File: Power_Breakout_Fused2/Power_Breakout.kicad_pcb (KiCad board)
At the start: 2 copper layers, 85.5 x 41.5 mm, 18 parts, among them J1 PS Conn, J2 Conn_01x02_Male, J3 PWR Out, J4 GND Out

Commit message: Generated Gerbers
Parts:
- moved REF** 1.44 mm to (191.9, 136.2), turned to 180 degrees
- turned REF** to 180 degrees
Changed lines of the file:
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@@
     (property "Sheetname" "")
     (attr through_hole)
-    (fp_text reference "J1" (at -42.116 -5.3014) (layer "F.SilkS")
-      (effects (font (size 0.640546 0.640546) (thickness 0.015)))
+    (fp_text reference "J1" (at -41.816 -5.7014 180 unlocked) (layer "F.SilkS")
+      (effects (font (size 1 1) (thickness 0.15)))
     )
     (fp_text value "PS Conn" (at -36.068 -5.588) (layer "F.Fab")
@@
       (net 1 "+12V") (pinfunction "Pin_64") (pintype "passive"))
     (model "${GIT_MODELS}/10046971001LFc.stp"
-      (offset (xyz 0 0 0))
+      (offset (xyz 0 0 5.5))
       (scale (xyz 1 1 1))
-      (rotate (xyz 0 0 0))
+      (rotate (xyz -90 0 0))
     )
   )
   (footprint "Symbol:OSHW-Logo2_9.8x8mm_SilkScreen" (layer "F.Cu")
-    (at 192.3 137.65)
+    (at 191.95 136.25 180)
     (descr "Open Source Hardware Symbol")
     (tags "Logo Symbol OSHW")
     (attr exclude_from_pos_files exclude_from_bom)
-    (fp_text reference "REF**" (at 0 0) (layer "F.SilkS") hide
+    (fp_text reference "REF**" (at -0.25 -1.35) (layer "F.SilkS") hide
       (effects (font (size 1 1) (thickness 0.15)))
     )
@@
       (effects (font (size 1 1) (thickness 0.15)))
     )
-    (fp_text value "GND Out" (at 17.8125 -5.9) (layer "F.SilkS")
+    (fp_text value "GND Out" (at 17.8125 -5.9 180 unlocked) (layer "F.SilkS")
       (effects (font (size 1.5 1.5) (thickness 0.3)))
     )
@@
     (pad "8" thru_hole oval (at 35.56 0) (size 1.8 3.6) (drill 1.2) (layers *.Cu *.Mask)
       (net 2 "GND") (pinfunction "Pin_8") (pintype "passive"))
-    (model "${KICAD6_3DMODEL_DIR}/Connector_Phoenix_MC_HighVoltage.3dshapes/PhoenixContact_MCV_1,5_8-G-5.08_1x08_P5.08mm_Vertical.wrl"
+    (model "${KICAD6_3DMODEL_DIR}/Connector_Phoenix_MC_HighVoltage.3dshapes/PhoenixContact_MCV_1,5_8-G-5.08_1x08_P5.08mm_Vertical.wrl" hide
       (offset (xyz 0 0 0))
       (scale (xyz 1 1 1))
       (rotate (xyz 0 0 0))
     )
+    (model "${KIPRJMOD}/libraries/3D Models/282834-8--3DModel-STEP-1.STEP"
+      (offset (xyz 17.5 5.5 3))
+      (scale (xyz 2 1 1.5))
+      (rotate (xyz -90 0 180))
+    )
   )
   (footprint "Symbol:KiCad-Logo2_6mm_SilkScreen" (layer "F.Cu")
-    (at 174.05 136.9)
+    (at 174.05 136.9 180)
     (descr "KiCad Logo")
     (tags "Logo KiCad")
@@
       (effects (font (size 1 1) (thickness 0.15)))
     )
-    (fp_text value "PWR Out" (at 17.85 -6.05) (layer "F.SilkS")
+    (fp_text value "PWR Out" (at 17.85 -6.05 180 unlocked) (layer "F.SilkS")
       (effects (font (size 1.5 1.5) (thickness 0.3)))
     )
@@
     (pad "8" thru_hole oval (at 35.56 0) (size 1.8 3.6) (drill 1.2) (layers *.Cu *.Mask)
       (net 10 "Net-(F8-Pad2_1)") (pinfunction "Pin_8") (pintype "passive"))
-    (model "${KICAD6_3DMODEL_DIR}/Connector_Phoenix_MC_HighVoltage.3dshapes/PhoenixContact_MCV_1,5_8-G-5.08_1x08_P5.08mm_Vertical.wrl"
+    (model "${KICAD6_3DMODEL_DIR}/Connector_Phoenix_MC_HighVoltage.3dshapes/PhoenixContact_MCV_1,5_8-G-5.08_1x08_P5.08mm_Vertical.wrl" hide
       (offset (xyz 0 0 0))
       (scale (xyz 1 1 1))
       (rotate (xyz 0 0 0))
     )
+    (model "${KIPRJMOD}/libraries/3D Models/282834-8--3DModel-STEP-1.STEP"
+      (offset (xyz 17 5.5 3))
+      (scale (xyz 2 1 1.5))
+      (rotate (xyz -90 0 180))
+    )
   )
   (footprint "3544-2:FUSE_3544-2" (layer "F.Cu")
@@
     (property "Sheetname" "")
     (attr through_hole)
-    (fp_text reference "F8" (at -8.18321 -1.55 180) (layer "F.SilkS")
+    (fp_text reference "F8" (at -8.18321 -1.55) (layer "F.SilkS")
       (effects (font (size 1 1) (thickness 0.05)))
     )
@@
     (property "Sheetname" "")
     (attr through_hole)
-    (fp_text reference "J2" (at 0 -2.33) (layer "F.SilkS")
+    (fp_text reference "J2" (at 0 5.075 180 unlocked) (layer "F.SilkS")
       (effects (font (size 1 1) (thickness 0.15)))
     )
@@
     (pad "2" thru_hole oval (at 0 2.54 180) (size 1.7 1.7) (drill 1) (layers *.Cu *.Mask)
       (net 24 "Net-(J2-Pad2)") (pinfunction "Pin_2") (pintype "passive"))
-    (model "${KICAD6_3DMODEL_DIR}/Connector_PinHeader_2.54mm.3dshapes/PinHeader_1x02_P2.54mm_Vertical.wrl"
+    (model "${KICAD6_3DMODEL_DIR}/Connector_PinHeader_2.54mm.3dshapes/PinHeader_1x02_P2.54mm_Vertical.wrl" hide
       (offset (xyz 0 0 0))
       (scale (xyz 1 1 1))
@@
   (gr_line (start 202.6158 161.9758) (end 202.6158 120.5) (layer "Edge.Cuts") (width 0.05))
   (gr_line (start 202.6158 120.5) (end 117.1194 120.5) (layer "Edge.Cuts") (width 0.05))
-  (gr_text "${TITLE} ${REVISION}\nby ${COMPANY}" (at 176.35 147.8) (layer "F.SilkS")
+  (gr_text "${TITLE} ${REVISION}\nby ${COMPANY}" (at 178.3 144.05 180) (layer "F.SilkS")
     (effects (font (size 1.5 1.5) (thickness 0.3)))
   )
@@
         (xy 202.65 162.45)
         (xy 152.6 162.4)
-        (xy 152.6 154.2)
-        (xy 160.05 154.2)
+        (xy 152.6 153.5)
+        (xy 160.05 153.5)
         (xy 160.05 120.5)
       )
@@
     (polygon
       (pts
-        (xy 159.2 153.2)
-        (xy 152.05 153.2)
+        (xy 159.2 152.75)
+        (xy 152.05 152.75)
         (xy 152.048439 162.476089)
         (xy 116.9 162.526089)

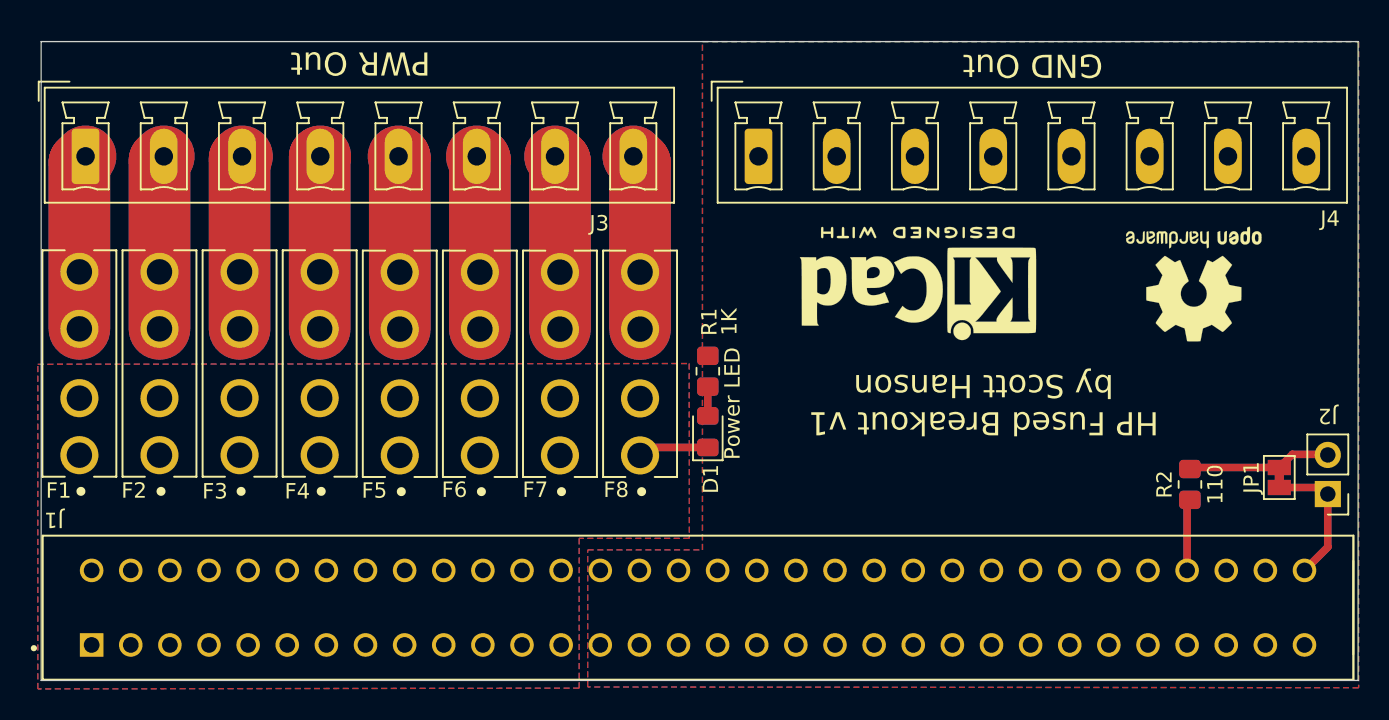
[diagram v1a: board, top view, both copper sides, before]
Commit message: added more leds
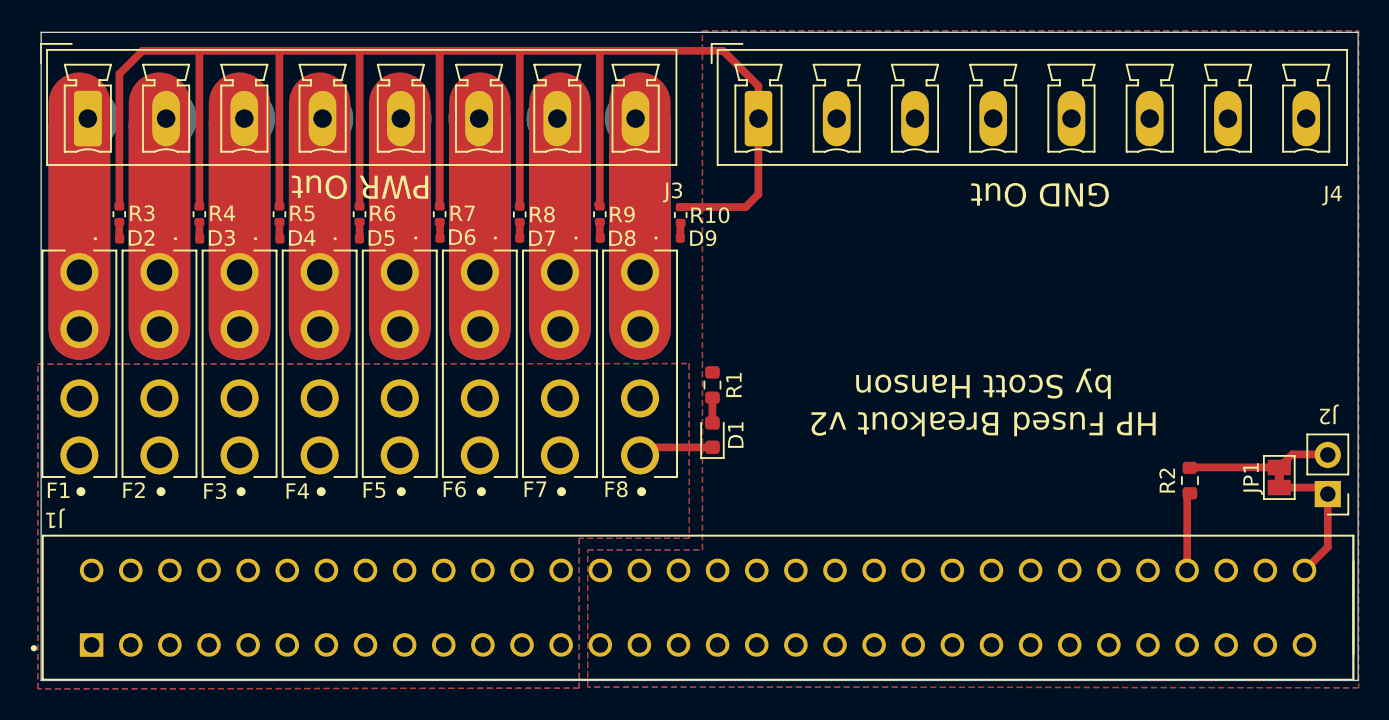
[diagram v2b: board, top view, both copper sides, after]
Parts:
- removed REF**: OSHW-Logo2_9.8x8mm_SilkScreen, Symbol:OSHW-Logo2_9.8x8mm_SilkScreen
- removed REF**: KiCad-Logo2_6mm_SilkScreen, Symbol:KiCad-Logo2_6mm_SilkScreen
- added D2: LED, LED_SMD:LED_0402_1005Metric, F.Cu at (121.7, 133.3)
- added D3: LED, LED_SMD:LED_0402_1005Metric, F.Cu at (126.9, 133.3)
- added D4: LED, LED_SMD:LED_0402_1005Metric, F.Cu at (132.1, 133.3)
- added D5: LED, LED_SMD:LED_0402_1005Metric, F.Cu at (137.3, 133.3)
- added D6: LED, LED_SMD:LED_0402_1005Metric, F.Cu at (142.5, 133.2)
- added D7: LED, LED_SMD:LED_0402_1005Metric, F.Cu at (147.7, 133.2)
- added D8: LED, LED_SMD:LED_0402_1005Metric, F.Cu at (152.9, 133.2)
- added D9: LED, LED_SMD:LED_0402_1005Metric, F.Cu at (158.1, 133.2)
- added R10: 2.2K, Resistor_SMD:R_0402_1005Metric, F.Cu at (158.6, 131.8)
- added R3: 2.2K, Resistor_SMD:R_0402_1005Metric, F.Cu at (122.2, 131.7)
- added R4: 2.2K, Resistor_SMD:R_0402_1005Metric, F.Cu at (127.4, 131.7)
- added R5: 2.2K, Resistor_SMD:R_0402_1005Metric, F.Cu at (132.6, 131.7)
- added R6: 2.2K, Resistor_SMD:R_0402_1005Metric, F.Cu at (137.8, 131.7)
- added R7: 2.2K, Resistor_SMD:R_0402_1005Metric, F.Cu at (143.0, 131.7)
- added R8: 2.2K, Resistor_SMD:R_0402_1005Metric, F.Cu at (148.2, 131.7)
- added R9: 2.2K, Resistor_SMD:R_0402_1005Metric, F.Cu at (153.4, 131.7)
- D1: footprint LED_SMD:LED_0805_2012Metric_Pad1.15x1.40mm_HandSolder -> LED_SMD:LED_0603_1608Metric
- R1: value 1K -> 2.2K; footprint Resistor_SMD:R_0805_2012Metric_Pad1.20x1.40mm_HandSolder -> Resistor_SMD:R_0603_1608Metric
- R2: value 110 -> 100; footprint Resistor_SMD:R_0805_2012Metric_Pad1.20x1.40mm_HandSolder -> Resistor_SMD:R_0603_1608Metric
- moved J3 2.45 mm to (120.2, 125.5)
- moved J4 2.45 mm to (163.7, 125.5)
- moved R1 0.95 mm to (160.7, 142.8)
- moved D1 0.38 mm to (160.7, 146.1)
- moved R2 0.25 mm to (191.7, 149.0)
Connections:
- net Net-(F1-Pad2_1) renamed PWR1
- net Net-(F2-Pad2_1) renamed PWR2
- net Net-(F3-Pad2_1) renamed PWR3
- net Net-(F4-Pad2_1) renamed PWR4
- net Net-(F5-Pad2_1) renamed PWR5
- net Net-(F6-Pad2_1) renamed PWR6
- net Net-(F7-Pad2_1) renamed PWR7
- net Net-(F8-Pad2_1) renamed PWR8
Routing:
- net GND: track 0.00 -> 125.1 mm
- net PWR4: track 22.4 -> 28.4 mm
- net PWR3: track 22.5 -> 28.4 mm
- net PWR2: track 22.6 -> 28.5 mm
- net PWR5: track 22.5 -> 28.4 mm
- net PWR1: track 22.7 -> 28.5 mm
- net PWR6: track 22.6 -> 28.4 mm
- net PWR7: track 22.7 -> 28.4 mm
- net PWR8: track 22.8 -> 28.5 mm
- net Net-(D4-A): track 0.00 -> 1.09 mm
- net Net-(D3-A): track 0.00 -> 1.09 mm
- net Net-(D2-A): track 0.00 -> 1.09 mm
- net Net-(D5-A): track 0.00 -> 1.08 mm
- net Net-(D8-A): track 0.00 -> 1.04 mm
- net Net-(D6-A): track 0.00 -> 1.04 mm
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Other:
- board size 85.5 x 41.5 mm -> 85.5 x 42.1 mm
- board text added: "GND Out"
- board text added: "PWR Out"

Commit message: move header
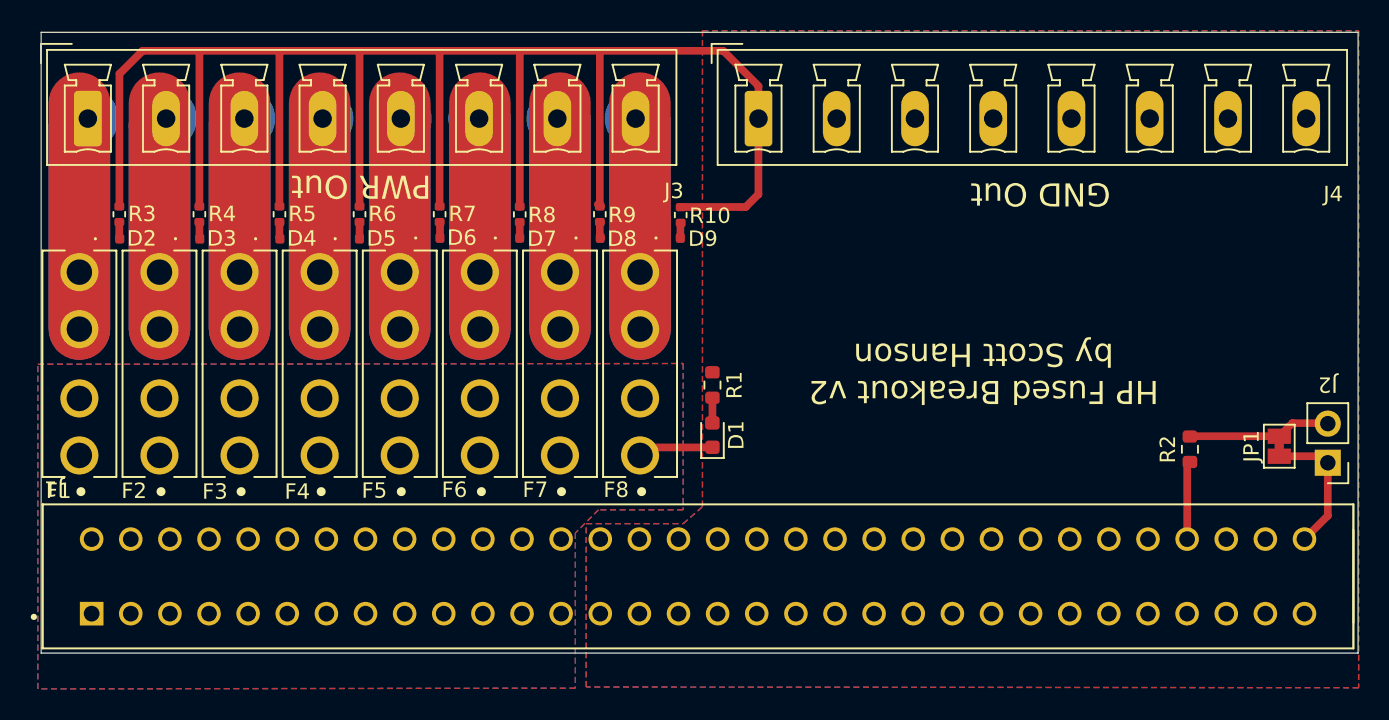
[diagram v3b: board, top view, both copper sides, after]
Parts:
- moved JP1 2.03 mm to (197.5, 146.8)
- moved J1 2.03 mm to (159.8, 155.2)
- moved J2 2.03 mm to (200.7, 147.8)
- moved R2 2.03 mm to (191.7, 147.0)
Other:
- board size 85.5 x 42.1 mm -> 85.5 x 40.3 mm
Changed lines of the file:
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@@
 	(footprint "Resistor_SMD:R_0603_1608Metric"
 		(layer "F.Cu")
-		(at 191.7 149 90)
+		(at 191.7 146.9686 90)
 		(descr "Resistor SMD 0603 (1608 Metric), square (rectangular) end terminal, IPC_7351 nominal, (Body size source: IPC-SM-782 page 72, https://www.pcb-3d.com/wordpress/wp-content/uploads/ipc-sm-782a_amendment_1_and_2.pdf), generated with kicad-footprint-generator")
 		(tags "resistor")
@@
 	(footprint "TE_1761469-1:TE_1761469-1"
 		(layer "F.Cu")
-		(at 159.766 157.2514)
+		(at 159.766 155.22)
 		(property "Reference" "J1"
 			(at -41.816 -5.7014 180)
@@
 		(tags "LED")
 		(property "Reference" "D3"
-			(at 1.91 -0.02 360)
+			(at 1.91 -0.02 0)
 			(layer "F.SilkS")
 			(effects
@@
 		)
 		(property "Value" "LED"
-			(at 0 1.17 360)
+			(at 0 1.17 0)
 			(layer "F.Fab")
 			(effects
@@
 		)
 		(fp_text user "${REFERENCE}"
-			(at 0 0 360)
+			(at 0 0 0)
 			(layer "F.Fab")
 			(effects
@@
 		(tags "LED")
 		(property "Reference" "D2"
-			(at 1.91 -0.02 360)
+			(at 1.91 -0.02 0)
 			(layer "F.SilkS")
 			(effects
@@
 		)
 		(property "Value" "LED"
-			(at 0 1.17 360)
+			(at 0 1.17 0)
 			(layer "F.Fab")
 			(effects
@@
 		)
 		(fp_text user "${REFERENCE}"
-			(at 0 0 360)
+			(at 0 0 0)
 			(layer "F.Fab")
 			(effects
@@
 		(tags "LED")
 		(property "Reference" "D5"
-			(at 1.91 -0.02 360)
+			(at 1.91 -0.02 0)
 			(layer "F.SilkS")
 			(effects
@@
 		)
 		(property "Value" "LED"
-			(at 0 1.17 360)
+			(at 0 1.17 0)
 			(layer "F.Fab")
 			(effects
@@
 		)
 		(fp_text user "${REFERENCE}"
-			(at 0 0 360)
+			(at 0 0 0)
 			(layer "F.Fab")
 			(effects
@@
 		(tags "LED")
 		(property "Reference" "D8"
-			(at 1.9 0.05 360)
+			(at 1.9 0.05 0)
 			(layer "F.SilkS")
 			(effects
@@
 		)
 		(property "Value" "LED"
-			(at 0 1.17 360)
+			(at 0 1.17 0)
 			(layer "F.Fab")
 			(effects
@@
 		)
 		(fp_text user "${REFERENCE}"
-			(at 0 0 360)
+			(at 0 0 0)
 			(layer "F.Fab")
 			(effects
@@
 		(tags "LED")
 		(property "Reference" "D4"
-			(at 1.91 -0.02 360)
+			(at 1.91 -0.02 0)
 			(layer "F.SilkS")
 			(effects
@@
 		)
 		(property "Value" "LED"
-			(at 0 1.17 360)
+			(at 0 1.17 0)
 			(layer "F.Fab")
 			(effects
@@
 		)
 		(fp_text user "${REFERENCE}"
-			(at 0 0 360)
+			(at 0 0 0)
 			(layer "F.Fab")
 			(effects
@@
 	(footprint "Connector_PinHeader_2.54mm:PinHeader_1x02_P2.54mm_Vertical"
 		(layer "F.Cu")
-		(at 200.65 149.875 180)
+		(at 200.65 147.8436 180)
 		(descr "Through hole straight pin header, 1x02, 2.54mm pitch, single row")
 		(tags "Through hole pin header THT 1x02 2.54mm single row")
@@
 	(footprint "Jumper:SolderJumper-2_P1.3mm_Bridged_Pad1.0x1.5mm"
 		(layer "F.Cu")
-		(at 197.5 148.8 90)
+		(at 197.5 146.7686 90)
 		(descr "SMD Solder Jumper, 1x1.5mm Pads, 0.3mm gap, bridged with 1 copper strip")
 		(tags "net tie solder jumper bridged")
@@
 		(tags "LED")
 		(property "Reference" "D7"
-			(at 1.9325 0.05 360)
+			(at 1.9325 0.05 0)
 			(layer "F.SilkS")
 			(effects
@@
 		)
 		(property "Value" "LED"
-			(at 0 1.17 360)
+			(at 0 1.17 0)
 			(layer "F.Fab")
 			(effects
@@
 		)
 		(fp_text user "${REFERENCE}"
-			(at 0 0 360)
+			(at 0 0 0)
 			(layer "F.Fab")
 			(effects
@@
 	(gr_line
 		(start 117.1194 119.9)
-		(end 117.1194 161.9758)
+		(end 117.1194 160.2)
 		(stroke
 			(width 0.05)
@@
 	)
 	(gr_line
-		(start 117.1194 161.9758)
-		(end 202.6158 161.9758)
+		(start 117.1194 160.2)
+		(end 202.6158 160.2)
 		(stroke
 			(width 0.05)
@@
 	)
 	(gr_line
-		(start 202.6158 161.9758)
+		(start 202.6158 160.2)
 		(end 202.6158 119.9)
 		(stroke
@@
 	)
 	(gr_text "${TITLE} ${REVISION}\nby ${COMPANY}"
-		(at 178.3 144.05 180)
+		(at 178.3 142.0186 180)
 		(layer "F.SilkS")
 		(effects
@@
 	)
 	(segment
-		(start 191.516 154.8314)
-		(end 191.516 150.009)
+		(start 191.516 152.8)
+		(end 191.516 147.9776)
 		(width 0.5)
 		(layer "F.Cu")
@@
 	)
 	(segment
-		(start 191.516 150.009)
-		(end 191.7 149.825)
+		(start 191.516 147.9776)
+		(end 191.7 147.7936)
 		(width 0.5)
 		(layer "F.Cu")
@@
 	)
 	(segment
-		(start 200.65 153.3174)
-		(end 199.136 154.8314)
+		(start 200.65 151.286)
+		(end 199.136 152.8)
 		(width 0.5)
 		(layer "F.Cu")
@@
 	)
 	(segment
-		(start 197.5 149.45)
-		(end 200.225 149.45)
+		(start 197.5 147.4186)
+		(end 200.225 147.4186)
 		(width 0.5)
 		(layer "F.Cu")
@@
 	)
 	(segment
-		(start 200.225 149.45)
-		(end 200.65 149.875)
+		(start 200.225 147.4186)
+		(end 200.65 147.8436)
 		(width 0.5)
 		(layer "F.Cu")
@@
 	)
 	(segment
-		(start 200.65 149.875)
-		(end 200.65 153.3174)
+		(start 200.65 147.8436)
+		(end 200.65 151.286)
 		(width 0.5)
 		(layer "F.Cu")
@@
 	)
 	(segment
-		(start 198.35 147.3)
-		(end 200.615 147.3)
+		(start 198.35 145.2686)
+		(end 200.615 145.2686)
 		(width 0.5)
 		(layer "F.Cu")
@@
 	)
 	(segment
-		(start 200.615 147.3)
-		(end 200.65 147.335)
+		(start 200.615 145.2686)
+		(end 200.65 145.3036)
 		(width 0.5)
 		(layer "F.Cu")
@@
 	)
 	(segment
-		(start 191.7 148.25)
-		(end 191.8 148.15)
+		(start 191.7 146.2186)
+		(end 191.8 146.1186)
 		(width 0.5)
 		(layer "F.Cu")
@@
 	)
 	(segment
-		(start 191.8 148.15)
-		(end 197.5 148.15)
+		(start 191.8 146.1186)
+		(end 197.5 146.1186)
 		(width 0.5)
 		(layer "F.Cu")
@@
 	)
 	(segment
-		(start 197.5 148.15)
-		(end 198.35 147.3)
+		(start 197.5 146.1186)
+		(end 198.35 145.2686)
 		(width 0.5)
 		(layer "F.Cu")
@@
 		(polygon
 			(pts
-				(xy 202.65 119.8) (xy 202.65 162.45) (xy 152.6 162.4) (xy 152.6 153.5) (xy 160.05 153.5) (xy 160.05 119.8)
+				(xy 202.65 119.8) (xy 202.65 162.45) (xy 152.5 162.4) (xy 152.5 151.8) (xy 158.8 151.8) (xy 160.05 150.7)
+				(xy 160.05 119.8)
 			)
 		)
@@
 		(polygon
 			(pts
-				(xy 159.2 152.75) (xy 152.05 152.75) (xy 152.048439 162.476089) (xy 116.9 162.526089) (xy 116.9 141.45)
-				(xy 159.190807 141.4)
+				(xy 158.8 150.9) (xy 153.3 150.9) (xy 151.8 152.4) (xy 151.8 162.476089) (xy 116.9 162.526089) (xy 116.9 141.45)
+				(xy 158.8 141.4)
 			)
 		)
